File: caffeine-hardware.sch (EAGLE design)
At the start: 31 parts, among them K1 PIN20X2, U1 EEPROM24

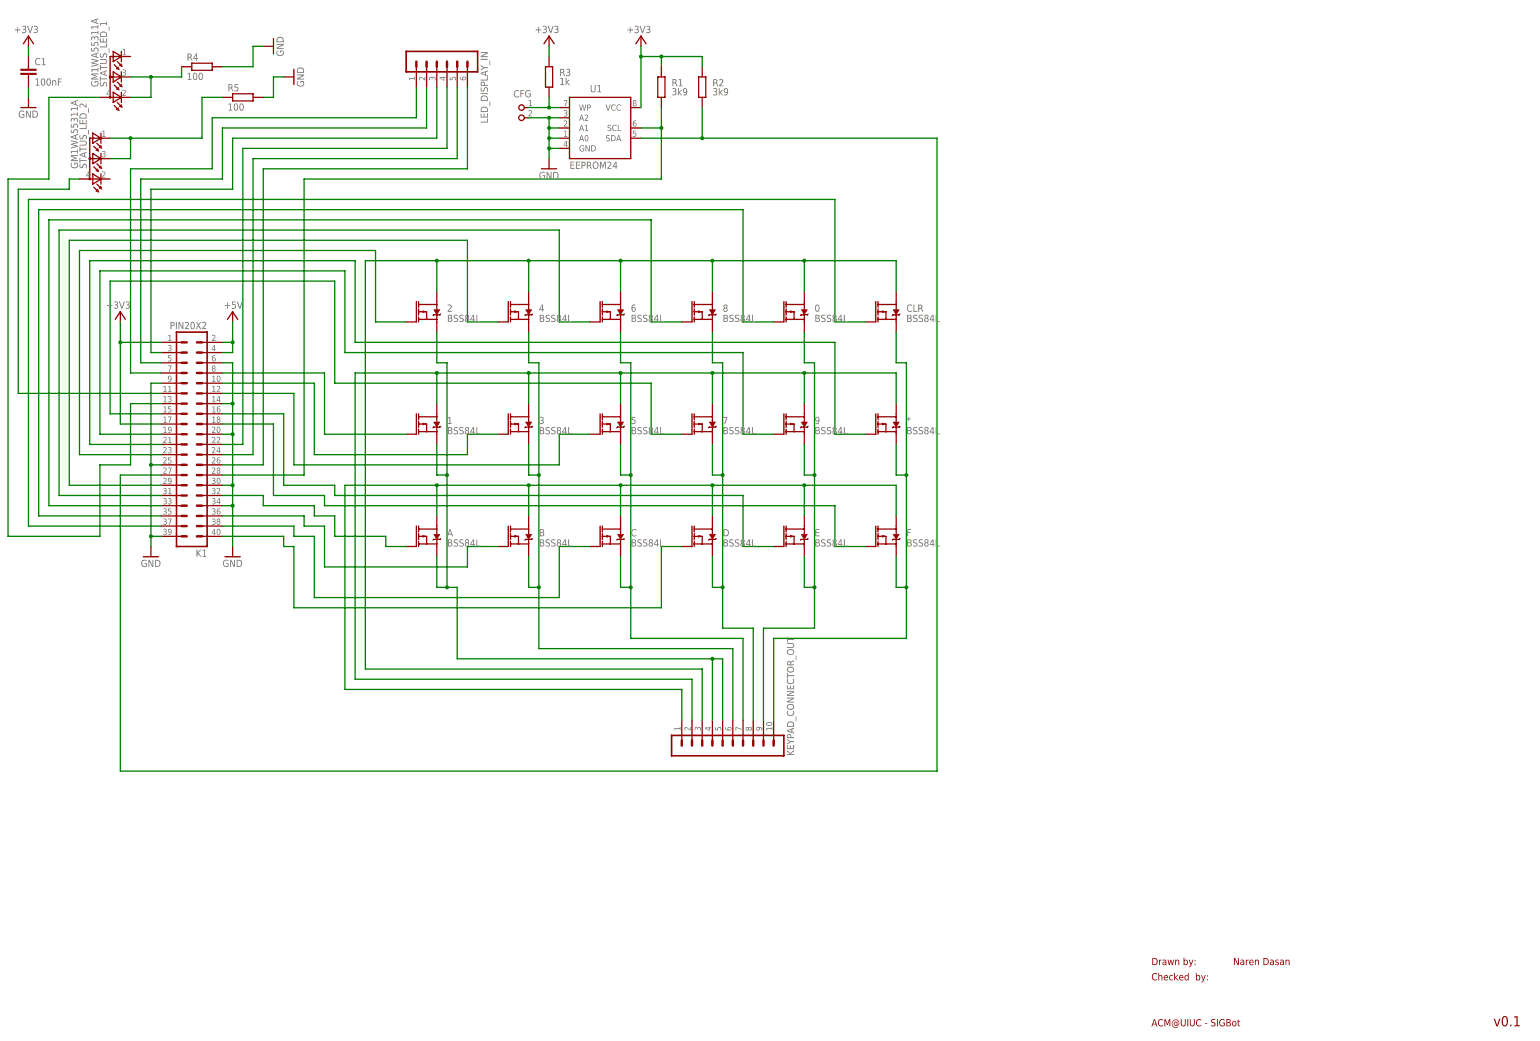
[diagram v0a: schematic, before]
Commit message: using decoders
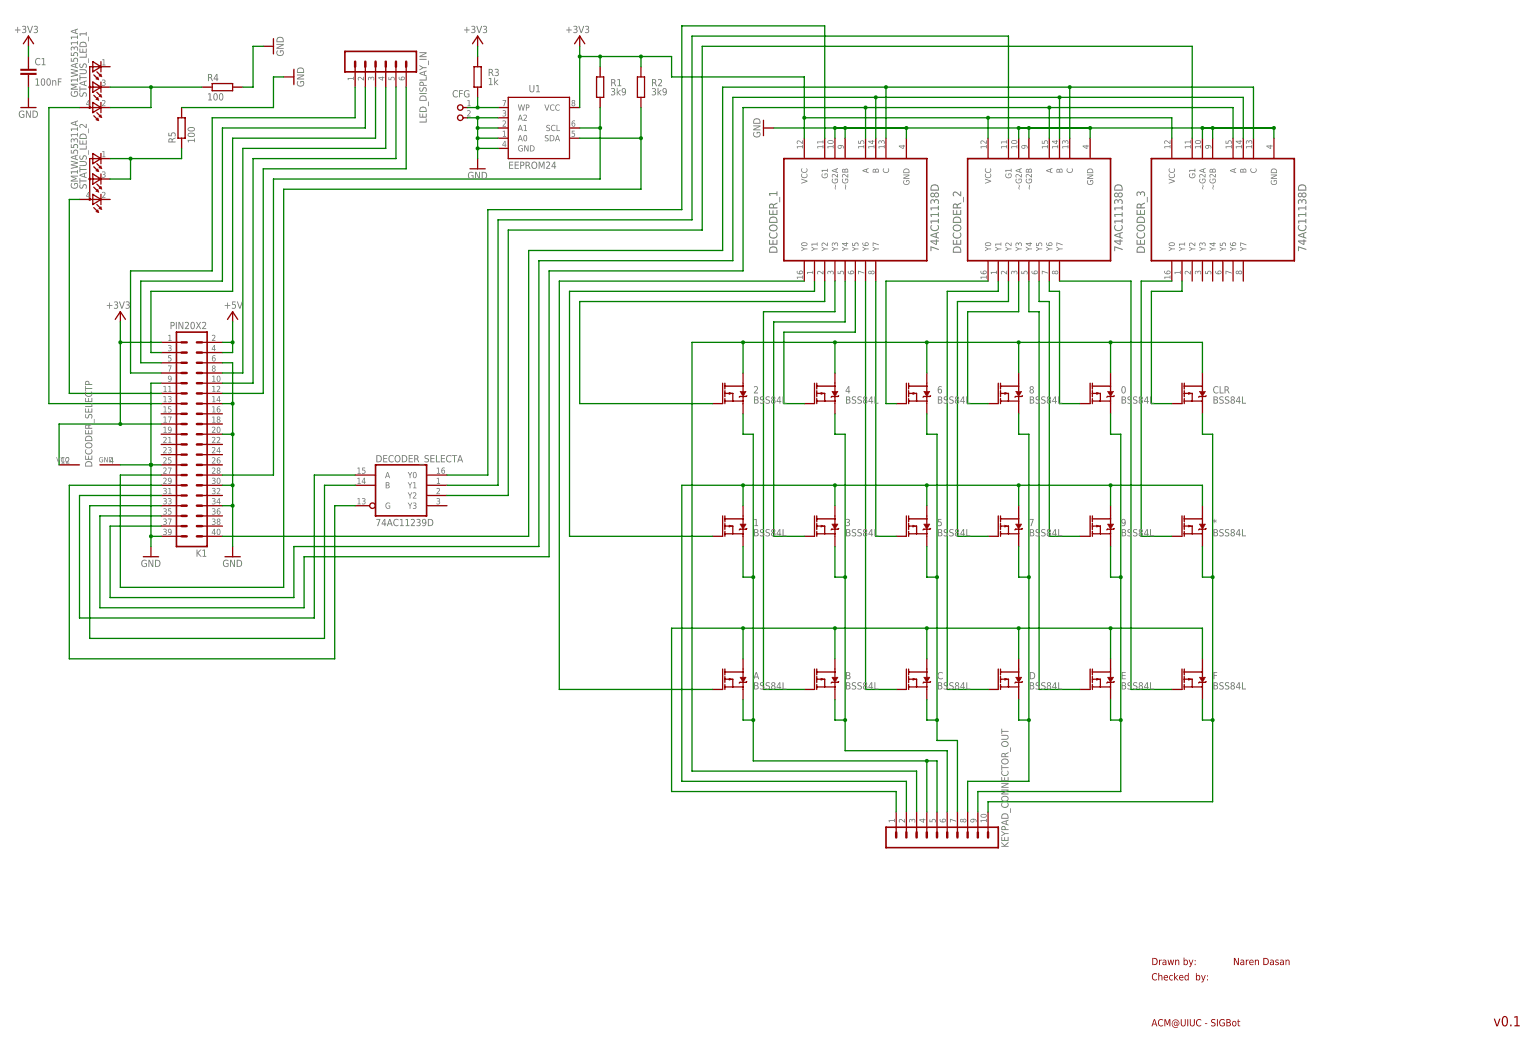
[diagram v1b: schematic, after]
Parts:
- added DECODER_1, DECODER_2, DECODER_3: 74AC11138D, Texas Instruments_By_element14_Batch_1:74AC11138D
- added DECODER_SELECT: 74AC11239D, 74ac-logic:74AC11239D
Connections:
- removed net N$21: 9.G, K1.19
- removed net N$8 (its old number): CLR.G, K1.37
- new net N$10: DECODER_1.G1, DECODER_SELECTA.Y0
- new net N$43: 6.G, DECODER_2.Y0
- new net N$44: D.G, DECODER_2.Y1
- new net N$45: 7.G, DECODER_2.Y2
- new net N$46: 8.G, DECODER_2.Y3
- new net N$47: DECODER_2.Y4, E.G
- new net N$48: 9.G, DECODER_2.Y5
- new net N$49: 0.G, DECODER_2.Y6
- new net N$50: DECODER_2.Y7, F.G
- new net N$51: *.G, DECODER_3.Y0
- new net N$52: CLR.G, DECODER_3.Y1
- net +3V3: now also DECODER_1.VCC, DECODER_2.VCC, DECODER_3.VCC, DECODER_SELECTP.VCC
- net GND: now also DECODER_1.GND, DECODER_1.~G2A, DECODER_1.~G2B, DECODER_2.GND, DECODER_2.~G2A, DECODER_2.~G2B, DECODER_3.GND, DECODER_3.~G2A, DECODER_3.~G2B, DECODER_SELECTP.GND
- net N$14: now also DECODER_SELECTA.B, K1.33; no longer 0.G, K1.35
- net N$15: now also DECODER_1.A, DECODER_2.A, DECODER_3.A, K1.35; no longer 8.G, K1.33
- net N$16: now also DECODER_1.B, DECODER_2.B, DECODER_3.B, K1.37; no longer 6.G, K1.31
- net N$17: now also DECODER_1.C, DECODER_2.C, DECODER_3.C, K1.40; no longer 4.G, K1.29
- net N$18: now also DECODER_SELECTA.A, K1.31; no longer 2.G, K1.23
- net N$19: now also DECODER_2.G1, DECODER_SELECTA.Y1; no longer 7.G, K1.15
- net N$20: now also DECODER_3.G1, DECODER_SELECTA.Y2; no longer *.G, K1.21
- net N$22: now also DECODER_SELECTA.G, K1.29; no longer 1.G, K1.8
- net N$23: now also A.G, DECODER_1.Y0; no longer 3.G, K1.10
- net N$24: now also 1.G, DECODER_1.Y1; no longer 5.G, K1.12
- net N$25: now also 2.G, DECODER_1.Y2; no longer F.G, K1.18
- net N$26: now also B.G, DECODER_1.Y3; no longer E.G, K1.16
- net N$27: now also 3.G, DECODER_1.Y4; no longer A.G, K1.32
- net N$28: now also 4.G, DECODER_1.Y5; no longer B.G, K1.36
- net N$29: now also DECODER_1.Y6; no longer K1.38
- net N$30: now also 5.G, DECODER_1.Y7; no longer D.G, K1.40
- net N$33: now also K1.8; no longer K1.22
- net N$35: now also K1.12; no longer K1.26
- net N$36: now also K1.10; no longer K1.24
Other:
- moved on the sheet: *, 0, 1, 2, 3, 4, 5, 6, 7, 8, 9, A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

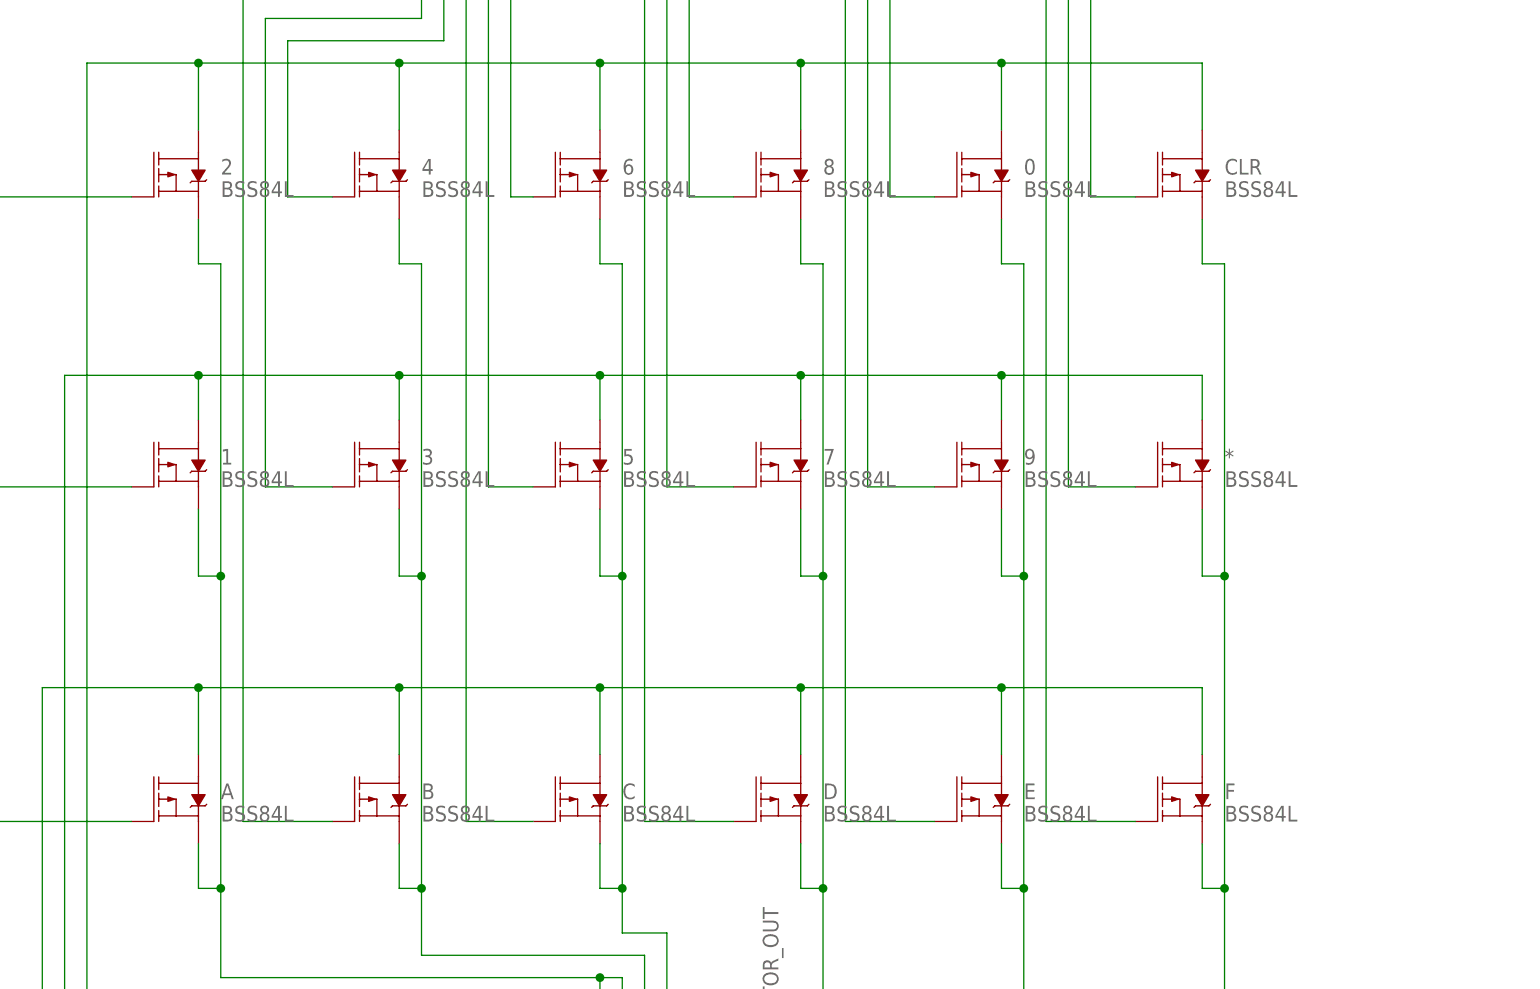
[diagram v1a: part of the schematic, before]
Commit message: using n channel
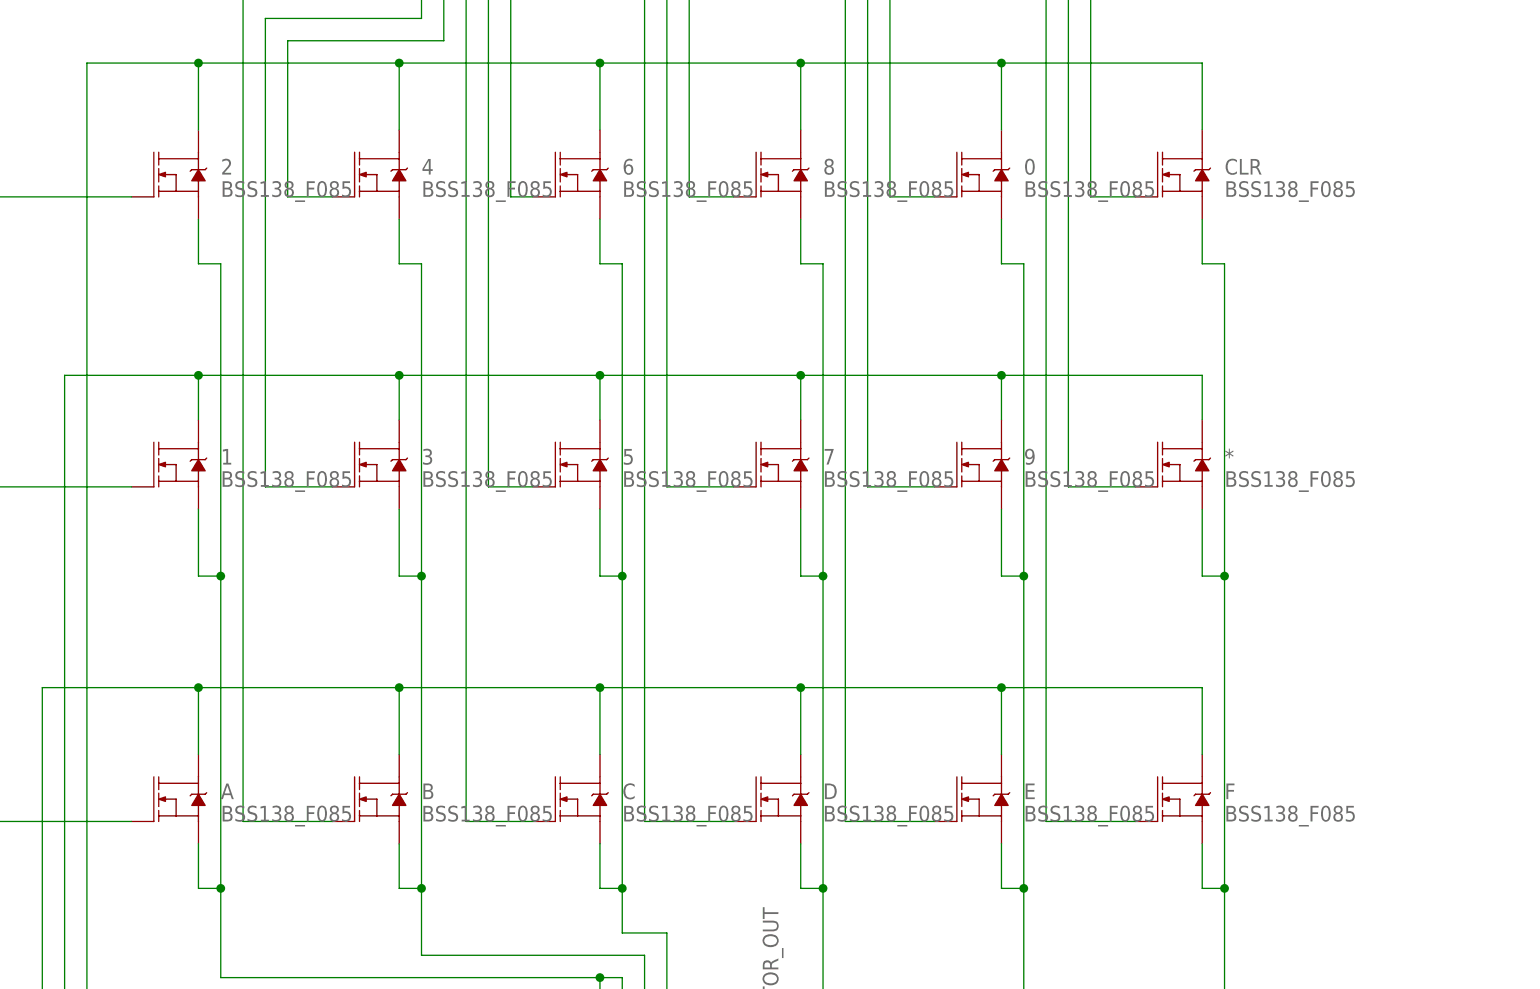
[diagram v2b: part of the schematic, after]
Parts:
- *, 0, 1, 2, 3, 4, 5, 6, 7, 8, 9, A, B, C, CLR, D, E, F: value BSS84L -> BSS138_F085; device SparkFun-DiscreteSemi:MOSFET-PCH-SI2309DS -> SparkFun-DiscreteSemi:MOSFET-NCH-AO3404A
